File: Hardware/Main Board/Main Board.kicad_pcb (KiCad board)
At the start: 4 copper layers, 71 x 57.5 mm, 70 parts, among them J1 Micro_SD_Card_Det1, J2 Camera Module, J3 Conn_01x09_Socket, J4 MIC 1 Connector, J5 MIC 2 Connector, J6 USB_C_Receptacle_USB2.0_16P, J7 OLED, Q1 AO3401A, SW1 SW_SPST, U1 ESP32-S3-WROOM-2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

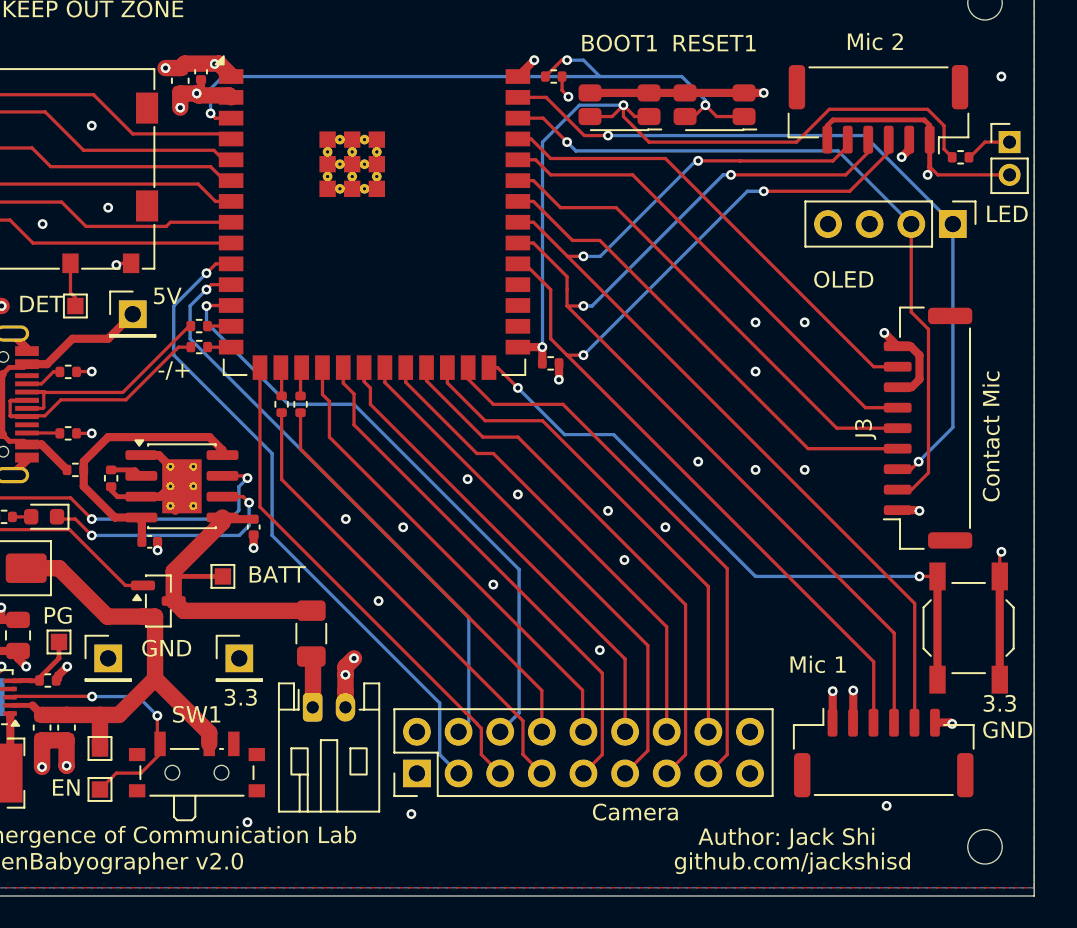
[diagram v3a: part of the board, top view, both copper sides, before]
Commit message: began board migration to newer integrated camera 24 pin connector, NOT FINISHED
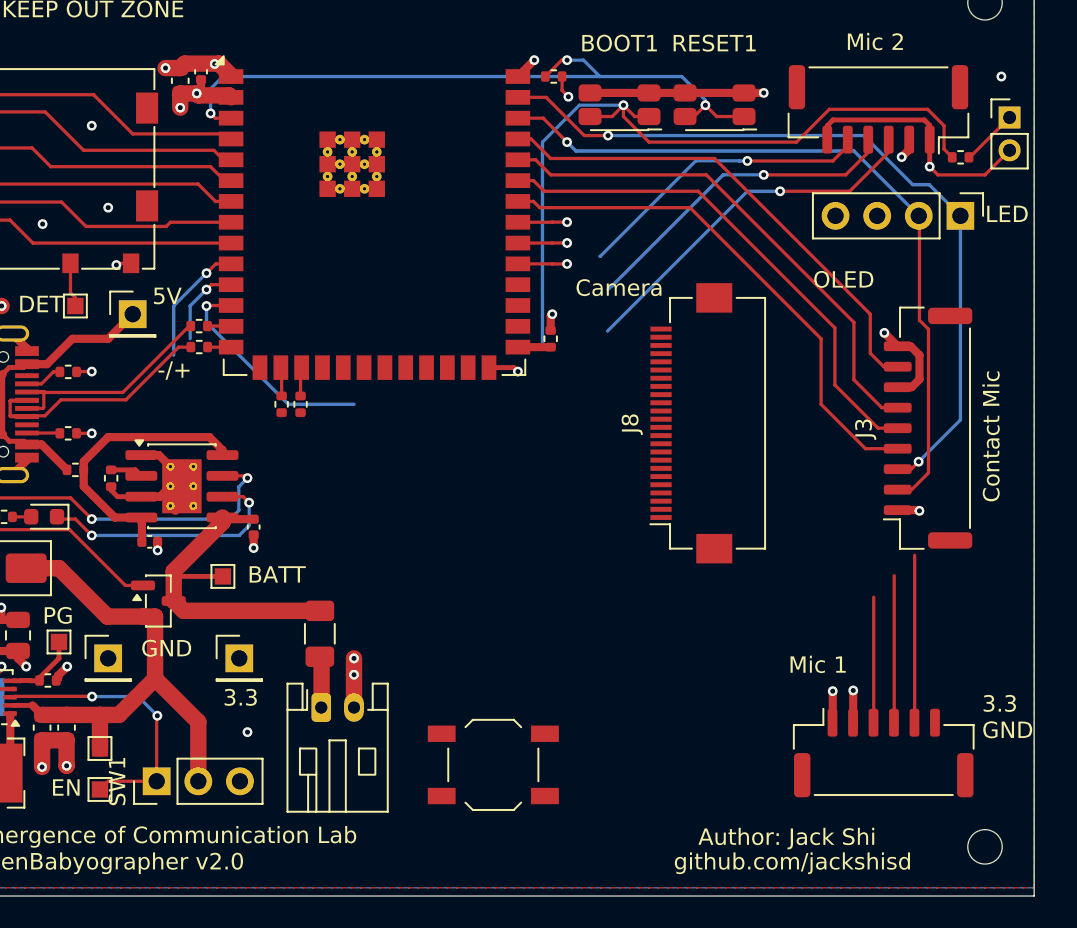
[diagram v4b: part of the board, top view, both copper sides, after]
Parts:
- removed J2: Camera Module, Connector_PinHeader_2.54mm:PinHeader_2x09_P2.54mm_Vertical
- added J8: Conn_02x12_Counter_Clockwise, Connector_FFC-FPC:Hirose_FH12-24S-0.5SH_1x24-1MP_P0.50mm_Horizontal, F.Cu at (123.6, 71.2)
- SW1: footprint Button_Switch_SMD:SW_SPDT_PCM12 -> Connector_PinHeader_2.54mm:PinHeader_1x03_P2.54mm_Vertical
- moved USER_INPUT1 30.2 mm to (111.5, 92.0), turned to 0 degrees
- moved SW1 2.60 mm to (91.0, 93.0), turned to 90 degrees
- moved D1 1.50 mm to (143.0, 52.5)
- moved R12 1.50 mm to (115.0, 66.0), turned to -90 degrees
- moved J7 0.68 mm to (140.0, 58.5)
- moved BT1 0.52 mm to (101.0, 88.5)
- moved F1 0.52 mm to (100.9, 84.0)
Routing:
- net Net-(U1-IO45): track 38.9 -> 1.86 mm, vias 2 -> 1
- net CAM_D1: track 34.3 -> 0.00 mm
- net CAM_D3: track 33.0 -> 0.00 mm
- net CAM_CLK: track 40.3 -> 7.56 mm
- net CAM_D5: track 32.0 -> 0.00 mm
- net CAM_D7: track 31.8 -> 0.00 mm
- net CAM_VSYNC: track 31.4 -> 0.00 mm
- net CAM_SIO_DAT: track 36.3 -> 5.04 mm
- net CAM_D0: track 30.9 -> 0.00 mm
- net MIC_DOUT: track 62.4 -> 32.1 mm
- net MIC_LCRL: track 61.4 -> 31.5 mm
- net MIC_BCLK: track 62.8 -> 33.1 mm
- net CAM_D2: track 29.4 -> 0.00 mm
- net CAM_D6: track 28.9 -> 0.00 mm
- net CAM_D4: track 28.8 -> 0.00 mm
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
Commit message: camera pcb
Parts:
- added C14: 0.1uF, Capacitor_SMD:C_0603_1608Metric, F.Cu at (175.0, 68.2)
- added C15: 0.1uF, Capacitor_SMD:C_0603_1608Metric, F.Cu at (175.0, 70.7)
- added C16: 0.1uF, Capacitor_SMD:C_0603_1608Metric, F.Cu at (175.0, 73.2)
- added C17: 0.1uF, Capacitor_SMD:C_0603_1608Metric, F.Cu at (175.0, 75.7)
- added C18: 1uF, Capacitor_SMD:C_0603_1608Metric, F.Cu at (175.0, 78.2)
- added C19: 1uF, Capacitor_SMD:C_0603_1608Metric, F.Cu at (175.0, 80.8)
- added C20: 1uF, Capacitor_SMD:C_0603_1608Metric, F.Cu at (175.0, 83.3)
- added C21: 1uF, Capacitor_SMD:C_0603_1608Metric, F.Cu at (175.0, 85.8)
- added CAM1: OV2640, OV2640:OV2640, F.Cu at (160.5, 79.5)
- added R20: 4.7K, Resistor_SMD:R_0402_1005Metric, F.Cu at (178.5, 67.9)
- added R25: 4.7K, Resistor_SMD:R_0402_1005Metric, F.Cu at (178.5, 69.9)
- added R26: 4.7K, Resistor_SMD:R_0402_1005Metric, F.Cu at (178.5, 71.9)
- added R27: 0, Resistor_SMD:R_0402_1005Metric, F.Cu at (178.5, 73.9)
- added U4: TLV75528PDBV, Package_TO_SOT_SMD:SOT-23-5, F.Cu at (175.6, 89.4)
- added U6: AP2112K-1.2, Package_TO_SOT_SMD:SOT-23-5, F.Cu at (175.6, 94.0)

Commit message: finished camera pcb
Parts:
- removed J8: Conn_02x12_Counter_Clockwise, Connector_FFC-FPC:Hirose_FH12-24S-0.5SH_1x24-1MP_P0.50mm_Horizontal
- removed R8: 22, Resistor_SMD:R_0402_1005Metric
- added 600Ω@100MHz1: FerriteBead, Resistor_SMD:R_0603_1608Metric, F.Cu at (1.50, 0.76)
- added FB: FerriteBead, Resistor_SMD:R_0603_1608Metric, F.Cu at (123.8, 62.8)
- added R28: 22, Resistor_SMD:R_0402_1005Metric, F.Cu at (106.5, 69.8)
- moved R27 62.6 mm to (116.0, 71.0), turned to -90 degrees
- moved C20 62.1 mm to (116.2, 63.2), turned to -90 degrees
- moved C21 61.3 mm to (118.0, 63.2), turned to -90 degrees
- moved U4 60.8 mm to (120.8, 63.2), turned to 90 degrees
- moved R25 59.5 mm to (119.0, 68.0), turned to 90 degrees
- moved C14 59.0 mm to (116.0, 68.2), turned to 180 degrees
- moved R26 58.1 mm to (120.5, 69.0)
- moved R20 58.0 mm to (120.5, 66.8)
- moved C17 56.4 mm to (118.8, 72.8), turned to 180 degrees
- moved C15 56.3 mm to (118.8, 71.2), turned to 180 degrees
- moved C18 51.3 mm to (124.0, 83.2), turned to -90 degrees
- moved C16 50.7 mm to (125.5, 62.2), turned to 90 degrees
- moved U6 49.7 mm to (126.8, 84.8), turned to -90 degrees
- moved C19 44.2 mm to (131.0, 84.2), turned to -90 degrees
- moved CAM1 19.4 mm to (142.3, 72.5), turned to -90 degrees
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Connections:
- R23 pad 1: Net-(U1-IO9) -> Net-(U1-IO47)
- U1 pad 15: CAM_VSYNC -> CAM_D0
- U1 pad 16: Net-(U1-IO46) -> CAM_D1
- U1 pad 17: Net-(U1-IO9) -> CAM_D4
- U1 pad 18: CAM_D6 -> CAM_D3
- U1 pad 19: CAM_D7 -> CAM_D5
- U1 pad 20: CAM_D4 -> CAM_D2
- U1 pad 21: CAM_D5 -> CAM_D6
- U1 pad 22: CAM_D2 -> Net-(U1-IO14)
- U1 pad 23: CAM_D3 -> CAM_D7
- U1 pad 24: CAM_D0 -> Net-(U1-IO47)
- U1 pad 25: CAM_D1 -> CAM_VSYNC
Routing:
- net +3.3V: track 45.9 -> 95.3 mm, vias 17 -> 18
- net GND: track 77.3 -> 125.4 mm, vias 33 -> 40
- net CAM_D0: track 0.00 -> 32.3 mm
- net CAM_D1: track 0.00 -> 31.0 mm
- net CAM_D4: track 0.00 -> 29.5 mm
- net CAM_D3: track 0.00 -> 27.9 mm
- net CAM_D5: track 0.00 -> 26.4 mm
- net 1.2V: track 0.00 -> 25.1 mm
- net CAM_D2: track 0.00 -> 25.0 mm
- net CAM_CLK: track 7.56 -> 31.5 mm, vias 1 -> 2
- net CAM_D6: track 0.00 -> 23.5 mm
- net CAM_HREF: track 13.6 -> 34.7 mm, vias 1 -> 2
- net CAM_D7: track 0.00 -> 20.3 mm
- net CAM_PCLK: track 0.00 -> 19.3 mm
- net CAM_XCLK: track 0.00 -> 16.1 mm
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
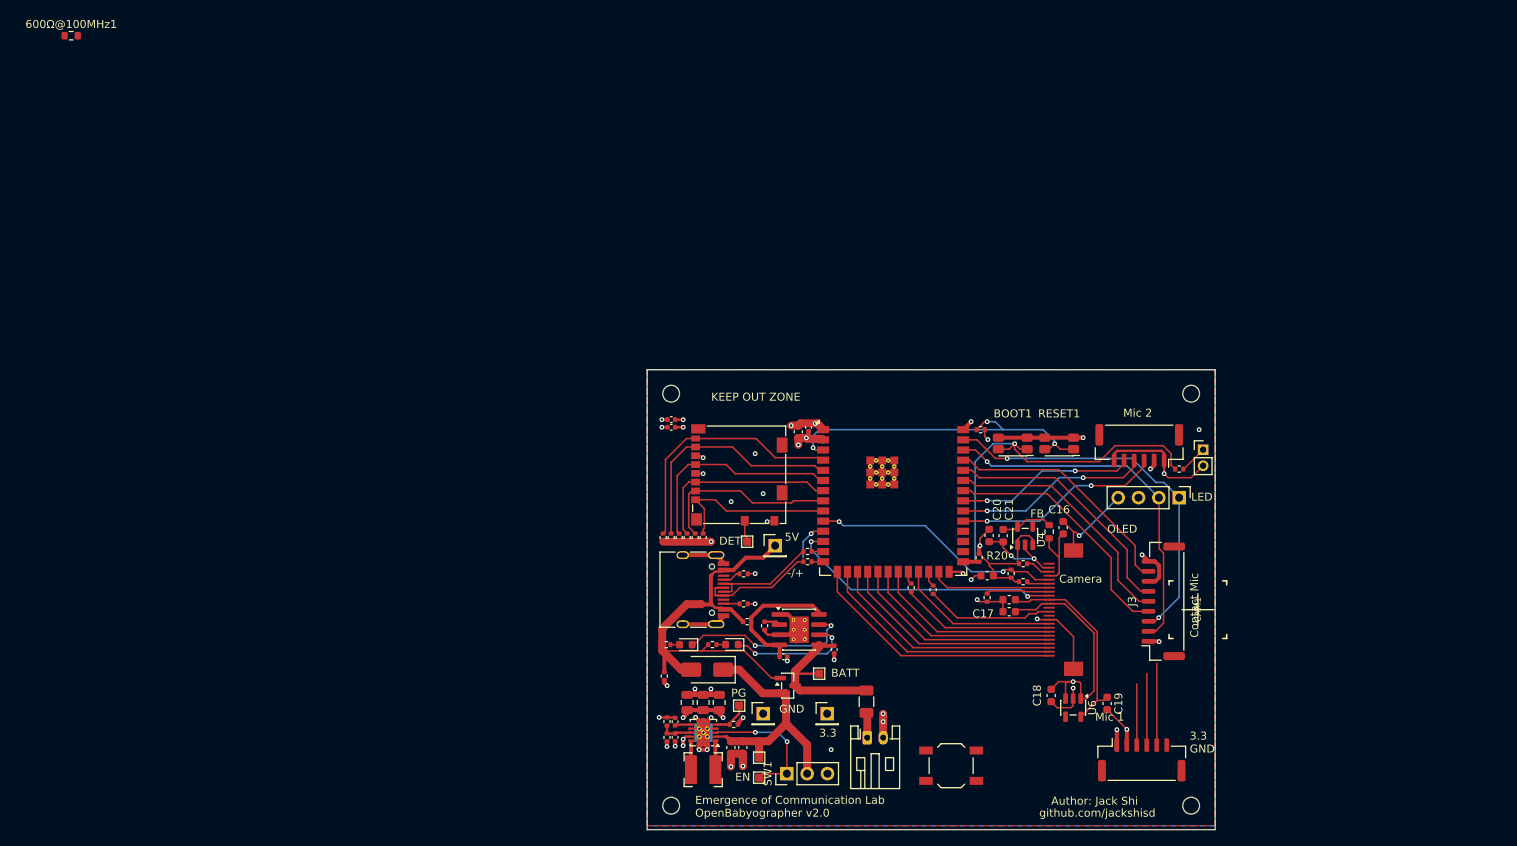
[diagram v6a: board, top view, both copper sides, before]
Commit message: reviewed kevin's layout, changed boot reset buttons and updated layout
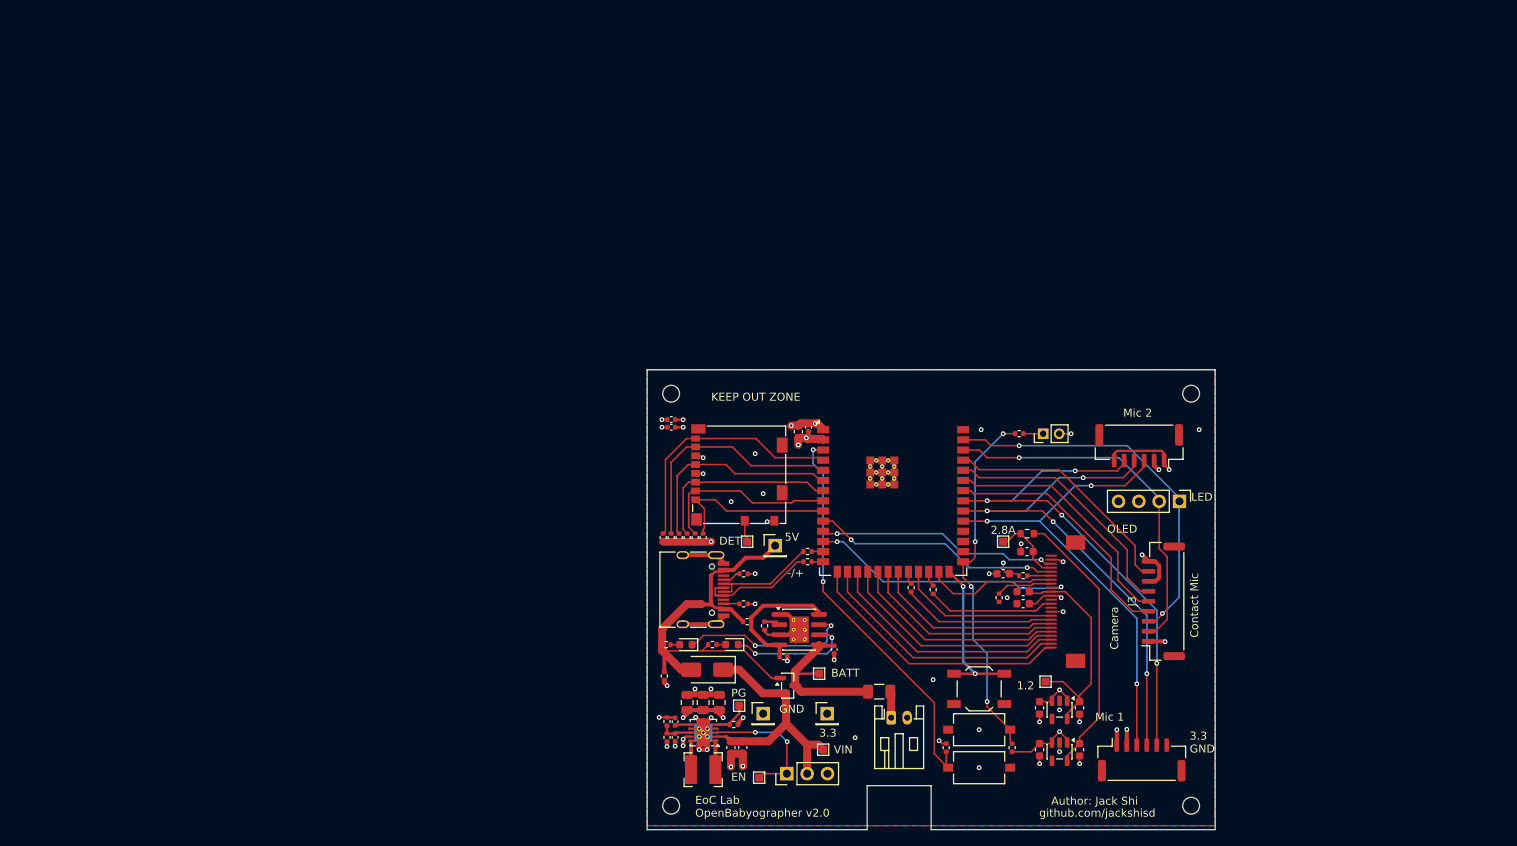
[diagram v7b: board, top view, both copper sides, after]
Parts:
- removed FB: FerriteBead, Resistor_SMD:R_0603_1608Metric
- removed R20, R25: 4.7K, Resistor_SMD:R_0402_1005Metric
- added 1.2: TestPoint, TestPoint:TestPoint_Pad_1.0x1.0mm, F.Cu at (123.3, 81.5)
- added 2.8A: TestPoint, TestPoint:TestPoint_Pad_1.0x1.0mm, F.Cu at (118.0, 64.0)
- BOOT1, RESET1: footprint Button_Switch_SMD:SW_SPST_EVQP7A -> Button_Switch_SMD:SW_Tactile_SPST_NO_Straight_CK_PTS636Sx25SMTRLFS
- moved 600Ω@100MHz1 134.7 mm to (121.0, 63.0), turned to 180 degrees
- moved RESET1 41.7 mm to (115.0, 92.2), turned to 0 degrees
- moved R1 40.0 mm to (110.9, 89.8), turned to -90 degrees
- moved BOOT1 36.0 mm to (115.0, 87.5)
- moved C21 28.4 mm to (127.5, 90.0)
- moved C20 27.5 mm to (122.5, 90.0)
- moved U4 27.3 mm to (125.0, 90.2), turned to -90 degrees
- moved R12 24.1 mm to (119.1, 89.8), turned to 90 degrees
- moved R11 20.5 mm to (120.0, 50.5)
- moved D1 20.1 mm to (123.0, 50.5), turned to 90 degrees
- moved USER_INPUT1 10.2 mm to (115.0, 82.4)
- moved VIN 8.06 mm to (95.5, 90.0)
- moved C16 5.43 mm to (121.0, 65.2), turned to 180 degrees
- moved BT1 3.91 mm to (104.0, 86.0)
- moved C19 3.49 mm to (127.5, 84.8)
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- renumbered TP4 to VIN
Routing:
- net GND: track 125.4 -> 71.7 mm, vias 40 -> 44
- net MIC_LCRL: track 32.7 -> 66.2 mm, vias 2 -> 4
- net +3.3V: track 95.3 -> 62.0 mm, vias 18 -> 21
- net MIC_DOUT: track 33.6 -> 66.2 mm, vias 2 -> 4
- net Net-(U4-OUT): track 6.64 -> 33.6 mm
- net MIC_BCLK: track 33.9 -> 59.2 mm, vias 2 -> 3
- net CAM_SIO_DAT: track 8.19 -> 30.2 mm, vias 1 -> 2
- net Net-(U1-IO45): track 1.86 -> 20.4 mm, vias 1 -> 2
- net Net-(U1-EN): track 42.6 -> 49.7 mm, vias 3 -> 2
- net Net-(U1-IO0): track 48.8 -> 45.0 mm, vias 1 -> 4
- net 1.2V: track 25.1 -> 28.8 mm
- net CAM_D0: track 32.3 -> 33.8 mm
- net CAM_D1: track 31.0 -> 32.3 mm
- net CAM_VSYNC: track 15.2 -> 16.5 mm
- net CAM_HREF: track 34.7 -> 33.6 mm
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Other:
- outline, holes or cut-outs redrawn
- board text added: "EoC Lab OpenBabyographer v2.0"
- board text removed: "Emergence of Communication Lab OpenBabyographer v2.0"
